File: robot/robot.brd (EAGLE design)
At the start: 58.1 x 41.9 mm, 12 parts, among them Q1 MOSFET-NCHANNELBSS138

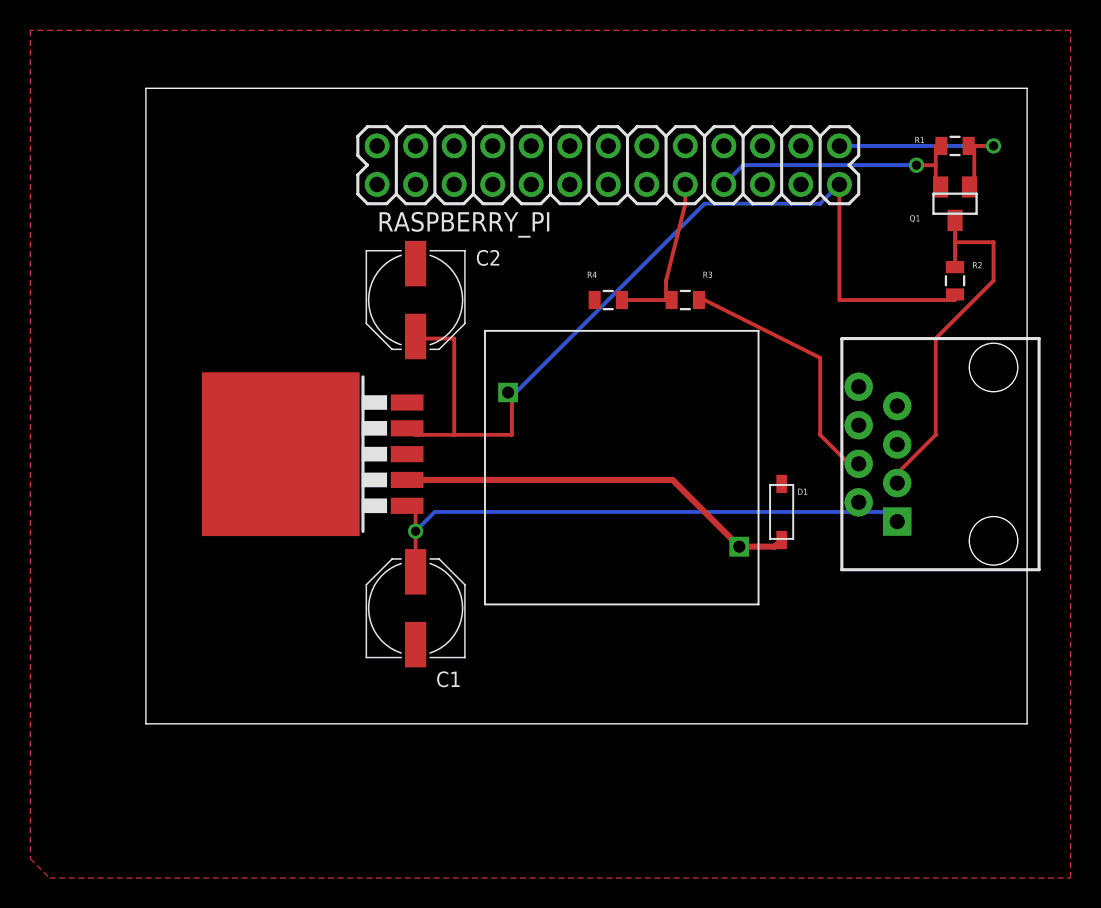
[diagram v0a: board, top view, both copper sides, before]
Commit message: Cleaning up the pcb
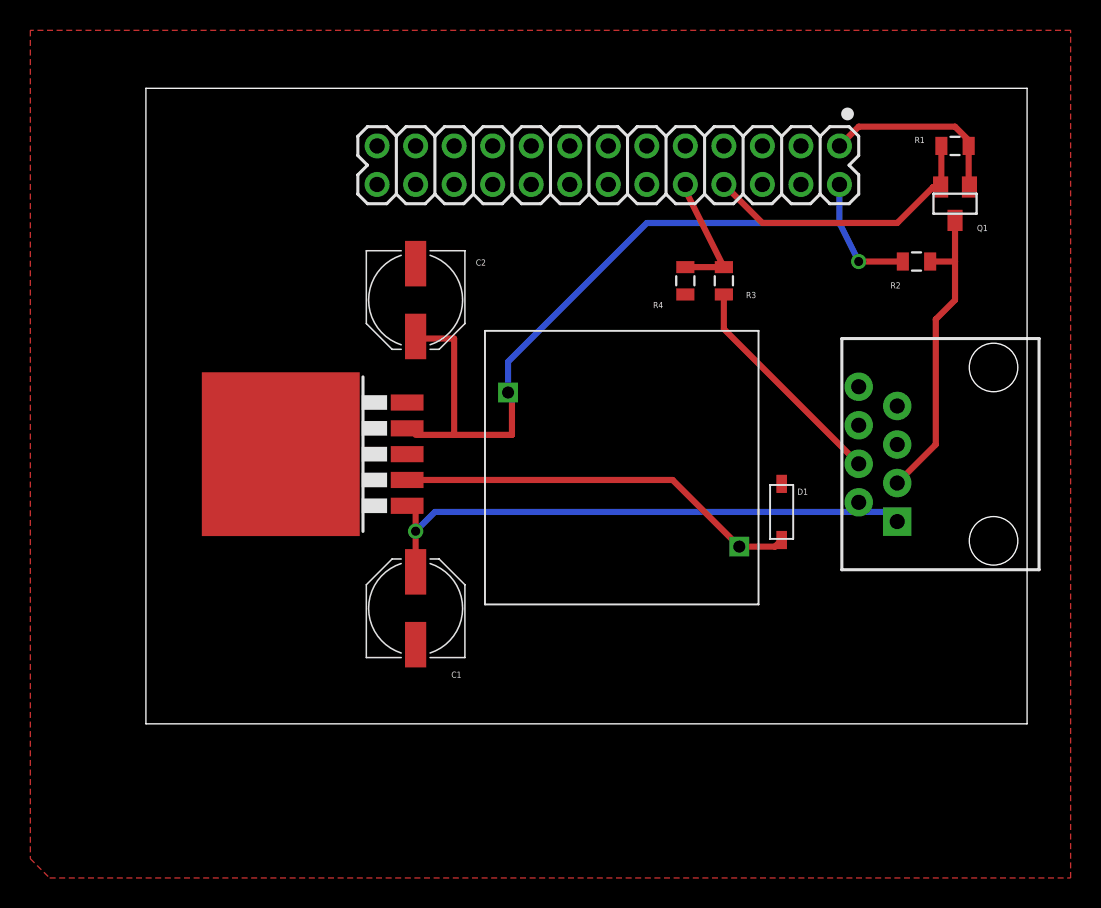
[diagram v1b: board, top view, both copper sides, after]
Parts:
- moved R4 5.24 mm to (38.1, 30.5), turned to 90 degrees
- moved R2 2.84 mm to (53.3, 31.8), turned to 180 degrees
- moved R3 2.84 mm to (40.6, 30.5), turned to 270 degrees
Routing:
- net HV: track 62.3 -> 55.3 mm, vias 0 -> 1
- net TX_HV: track 24.1 -> 20.5 mm
- net RX_HV: track 18.2 -> 15.5 mm
- net RX_LV: track 11.1 -> 8.59 mm
- net LV: track 14.7 -> 12.9 mm, vias 1 -> 0
- net TX_LV: track 17.8 -> 19.1 mm, vias 1 -> 0

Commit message: Made board shorter
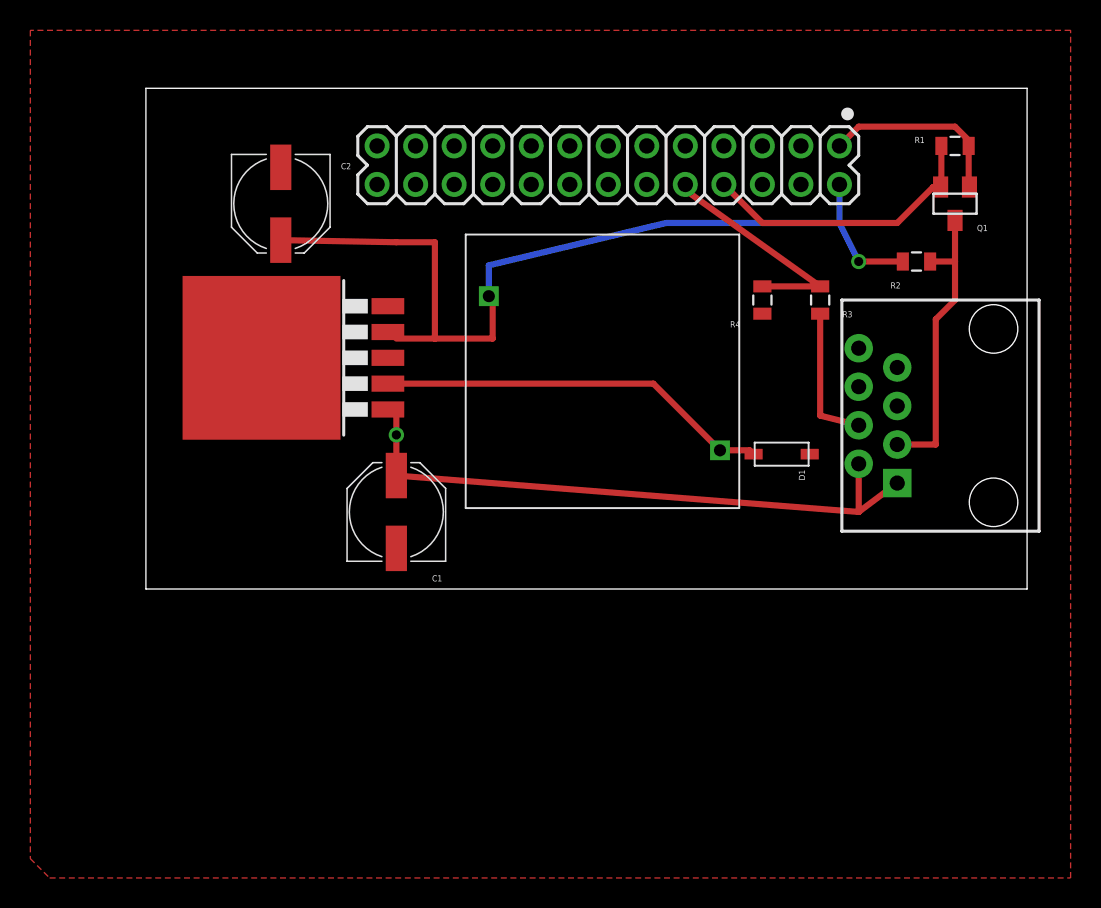
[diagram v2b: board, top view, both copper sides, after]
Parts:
- moved C2 10.9 mm to (11.4, 35.6)
- moved R3 6.48 mm to (47.0, 29.2)
- moved C1 6.48 mm to (19.1, 15.2)
- moved U$1 6.48 mm to (10.2, 25.4)
- moved U$2 6.48 mm to (33.0, 24.1)
- moved R4 5.24 mm to (43.2, 29.2)
- moved D1 3.81 mm to (44.5, 19.1), turned to 0 degrees
- moved IROBOT 2.54 mm to (58.4, 21.6)
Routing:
- net RX_LV: track 8.59 -> 15.1 mm
- net RX_HV: track 15.5 -> 9.34 mm
- net HV: track 55.3 -> 60.6 mm
- net UNREG_12V: track 38.2 -> 41.6 mm
- net TX_HV: track 20.5 -> 19.5 mm
- net N$1: track 26.7 -> 26.0 mm
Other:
- board size 58.1 x 41.9 mm -> 58.1 x 33 mm
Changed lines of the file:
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@@
 <board>
 <plain>
-<wire x1="2.54" y1="1.27" x2="60.63" y2="1.27" width="0" layer="20"/>
-<wire x1="60.63" y1="1.27" x2="60.63" y2="43.17" width="0" layer="20"/>
+<wire x1="2.54" y1="10.16" x2="60.63" y2="10.16" width="0" layer="20"/>
+<wire x1="60.63" y1="10.16" x2="60.63" y2="43.17" width="0" layer="20"/>
 <wire x1="60.63" y1="43.17" x2="2.54" y2="43.17" width="0" layer="20"/>
-<wire x1="2.54" y1="43.17" x2="2.54" y2="1.27" width="0" layer="20"/>
+<wire x1="2.54" y1="43.17" x2="2.54" y2="10.16" width="0" layer="20"/>
 <circle x="48.7934" y="41.4782" radius="0.218496875" width="0.4064" layer="21"/>
 </plain>
@@
 </autorouter>
 <elements>
-<element name="U$1" library="TL2575" package="TO-263" value="TL2575" x="11.43" y="19.05" smashed="yes" rot="R90"/>
-<element name="C1" library="SparkFun-Capacitors" package="PANASONIC_D" value="47uF" x="20.32" y="8.89" smashed="yes" rot="R90">
-<attribute name="NAME" x="23.34" y="4.715" size="0.4064" layer="25" rot="R180"/>
-</element>
-<element name="C2" library="SparkFun-Passives" package="PANASONIC_D" value="220uF" x="20.32" y="29.21" smashed="yes" rot="R270">
-<attribute name="NAME" x="24.285" y="31.48" size="0.4064" layer="25"/>
-</element>
-<element name="U$2" library="PE-52627NL" package="PE-52627NL" value="PE-52627NL" x="34.29" y="17.78" rot="R90"/>
-<element name="D1" library="adafruit" package="SOD-123" value="1A" x="44.45" y="15.24" smashed="yes" rot="R90">
-<attribute name="NAME" x="46.185" y="16.78" size="0.4064" layer="25" rot="R180"/>
-</element>
-<element name="IROBOT" library="SparkFun-Connectors" package="RJ45-8" value="RJ45-8PTH" x="58.42" y="19.05" rot="R90"/>
+<element name="U$1" library="TL2575" package="TO-263" value="TL2575" x="10.16" y="25.4" smashed="yes" rot="R90"/>
+<element name="C1" library="SparkFun-Capacitors" package="PANASONIC_D" value="47uF" x="19.05" y="15.24" smashed="yes" rot="R90">
+<attribute name="NAME" x="22.07" y="11.065" size="0.4064" layer="25" rot="R180"/>
+</element>
+<element name="C2" library="SparkFun-Passives" package="PANASONIC_D" value="220uF" x="11.43" y="35.56" smashed="yes" rot="R270">
+<attribute name="NAME" x="15.395" y="37.83" size="0.4064" layer="25"/>
+</element>
+<element name="U$2" library="PE-52627NL" package="PE-52627NL" value="PE-52627NL" x="33.02" y="24.13" rot="R90"/>
+<element name="D1" library="adafruit" package="SOD-123" value="1A" x="44.45" y="19.05" smashed="yes">
+<attribute name="NAME" x="45.99" y="17.315" size="0.4064" layer="25" rot="R90"/>
+</element>
+<element name="IROBOT" library="SparkFun-Connectors" package="RJ45-8" value="RJ45-8PTH" x="58.42" y="21.59" rot="R90"/>
 <element name="RASPBERRY_PI" library="SparkFun-Connectors" package="2X13" value="M13X22X13" x="48.26" y="39.37" smashed="yes" rot="R180"/>
 <element name="R1" library="SparkFun-Resistors" package="0805" value="10K" x="55.88" y="39.37" smashed="yes">
@@
 <attribute name="NAME" x="51.6255" y="29.972" size="0.4064" layer="25"/>
 </element>
-<element name="R3" library="SparkFun-Resistors" package="0805" value="10K" x="40.64" y="30.48" smashed="yes" rot="R270">
-<attribute name="NAME" x="42.1005" y="29.337" size="0.4064" layer="25"/>
-</element>
-<element name="R4" library="SparkFun-Resistors" package="0805" value="10K" x="38.1" y="30.48" smashed="yes" rot="R90">
-<attribute name="NAME" x="36.6395" y="29.083" size="0.4064" layer="25" rot="R180"/>
+<element name="R3" library="SparkFun-Resistors" package="0805" value="10K" x="46.99" y="29.21" smashed="yes" rot="R270">
+<attribute name="NAME" x="48.4505" y="28.067" size="0.4064" layer="25"/>
+</element>
+<element name="R4" library="SparkFun-Resistors" package="0805" value="10K" x="43.18" y="29.21" smashed="yes" rot="R90">
+<attribute name="NAME" x="41.7195" y="27.813" size="0.4064" layer="25" rot="R180"/>
 </element>
 <element name="Q1" library="SparkFun-DiscreteSemi" package="SOT23" value="MOSFET-NCHANNELBSS138" x="55.88" y="35.56" smashed="yes" rot="R180">
@@
 <contactref element="IROBOT" pad="1"/>
 <contactref element="IROBOT" pad="2"/>
-<wire x1="20.32" y1="11.29" x2="20.32" y2="13.97" width="0.4064" layer="1"/>
-<wire x1="20.32" y1="13.97" x2="20.32" y2="15.24" width="0.4064" layer="1"/>
-<wire x1="20.32" y1="15.24" x2="19.7612" y2="15.6464" width="0.254" layer="1"/>
-<wire x1="52.07" y1="15.24" x2="49.53" y2="15.24" width="0.4064" layer="16"/>
-<wire x1="52.07" y1="15.24" x2="52.07" y2="14.605" width="0.4064" layer="16"/>
-<wire x1="21.59" y1="15.24" x2="20.32" y2="13.97" width="0.4064" layer="16"/>
-<wire x1="49.53" y1="15.24" x2="21.59" y2="15.24" width="0.4064" layer="16"/>
-<wire x1="49.53" y1="15.24" x2="49.53" y2="15.875" width="0.4064" layer="16"/>
-<via x="20.32" y="13.97" extent="1-16" drill="0.6096"/>
+<wire x1="19.05" y1="17.64" x2="19.05" y2="20.32" width="0.4064" layer="1"/>
+<wire x1="19.05" y1="20.32" x2="19.05" y2="21.59" width="0.4064" layer="1"/>
+<wire x1="19.05" y1="21.59" x2="18.4912" y2="21.9964" width="0.254" layer="1"/>
+<via x="19.05" y="20.32" extent="1-16" drill="0.6096"/>
+<wire x1="19.05" y1="17.64" x2="49.53" y2="15.24" width="0.4064" layer="1"/>
+<wire x1="49.53" y1="15.24" x2="49.53" y2="18.415" width="0.4064" layer="1"/>
+<wire x1="52.07" y1="17.145" x2="49.53" y2="15.24" width="0.4064" layer="1"/>
 </signal>
 <signal name="GND">
@@
 <contactref element="D1" pad="C"/>
 <contactref element="U$2" pad="P$1"/>
-<wire x1="19.7612" y1="17.3482" x2="37.2618" y2="17.3482" width="0.4064" layer="1"/>
-<wire x1="37.2618" y1="17.3482" x2="41.656" y2="12.954" width="0.4064" layer="1"/>
-<wire x1="41.656" y1="12.954" x2="44.014" y2="12.954" width="0.4064" layer="1"/>
-<wire x1="44.014" y1="12.954" x2="44.45" y2="13.39" width="0.4064" layer="1"/>
+<wire x1="18.4912" y1="23.6982" x2="35.9918" y2="23.6982" width="0.4064" layer="1"/>
+<wire x1="35.9918" y1="23.6982" x2="40.386" y2="19.304" width="0.4064" layer="1"/>
+<wire x1="40.386" y1="19.304" x2="42.346" y2="19.304" width="0.4064" layer="1"/>
+<wire x1="42.346" y1="19.304" x2="42.6" y2="19.05" width="0.4064" layer="1"/>
 </signal>
 <signal name="RX_LV">
@@
 <contactref element="R4" pad="2"/>
 <contactref element="RASPBERRY_PI" pad="10"/>
-<wire x1="40.64" y1="31.38" x2="38.1" y2="31.38" width="0.4064" layer="1"/>
-<wire x1="40.64" y1="31.38" x2="38.1" y2="36.46" width="0.4064" layer="1"/>
+<wire x1="46.99" y1="30.11" x2="43.18" y2="30.11" width="0.4064" layer="1"/>
+<wire x1="46.99" y1="30.11" x2="38.1" y2="36.46" width="0.4064" layer="1"/>
 <wire x1="38.1" y1="36.46" x2="38.1" y2="36.83" width="0.4064" layer="1"/>
 </signal>
@@
 <wire x1="55.88" y1="29.21" x2="54.61" y2="27.94" width="0.4064" layer="1"/>
 <wire x1="54.61" y1="27.94" x2="54.61" y2="19.685" width="0.4064" layer="1"/>
-<wire x1="54.61" y1="19.685" x2="52.07" y2="17.145" width="0.4064" layer="1"/>
+<wire x1="54.61" y1="19.685" x2="52.07" y2="19.685" width="0.4064" layer="1"/>
 <wire x1="55.88" y1="34.46" x2="55.88" y2="31.75" width="0.4064" layer="1"/>
 <wire x1="55.88" y1="31.75" x2="54.24" y2="31.75" width="0.4064" layer="1"/>
@@
 <contactref element="C2" pad="+"/>
 <contactref element="U$2" pad="P$2"/>
-<wire x1="26.67" y1="20.32" x2="22.86" y2="20.32" width="0.4064" layer="1"/>
-<wire x1="22.86" y1="20.32" x2="20.32" y2="20.32" width="0.4064" layer="1"/>
-<wire x1="26.67" y1="22.86" x2="26.67" y2="20.32" width="0.4064" layer="1"/>
-<wire x1="20.32" y1="20.32" x2="19.7612" y2="20.7518" width="0.254" layer="1"/>
-<wire x1="26.67" y1="22.86" x2="26.416" y2="23.114" width="0.4064" layer="1"/>
-<wire x1="22.86" y1="26.67" x2="20.32" y2="26.67" width="0.4064" layer="1"/>
-<wire x1="22.86" y1="20.32" x2="22.86" y2="26.67" width="0.4064" layer="1"/>
-<wire x1="20.32" y1="26.67" x2="20.32" y2="26.81" width="0.254" layer="1"/>
-<wire x1="26.67" y1="22.86" x2="26.416" y2="23.114" width="0.254" layer="16"/>
+<wire x1="25.4" y1="26.67" x2="21.59" y2="26.67" width="0.4064" layer="1"/>
+<wire x1="21.59" y1="26.67" x2="19.05" y2="26.67" width="0.4064" layer="1"/>
+<wire x1="25.4" y1="29.21" x2="25.4" y2="26.67" width="0.4064" layer="1"/>
+<wire x1="19.05" y1="26.67" x2="18.4912" y2="27.1018" width="0.254" layer="1"/>
+<wire x1="25.4" y1="29.21" x2="25.146" y2="29.464" width="0.4064" layer="1"/>
+<wire x1="21.59" y1="33.02" x2="19.05" y2="33.02" width="0.4064" layer="1"/>
+<wire x1="21.59" y1="26.67" x2="21.59" y2="33.02" width="0.4064" layer="1"/>
+<wire x1="19.05" y1="33.02" x2="11.43" y2="33.16" width="0.4064" layer="1"/>
+<wire x1="25.4" y1="29.21" x2="25.146" y2="29.464" width="0.254" layer="16"/>
 <wire x1="52.44" y1="31.75" x2="49.53" y2="31.75" width="0.4064" layer="1"/>
 <via x="49.53" y="31.75" extent="1-16" drill="0.6"/>
 <wire x1="49.53" y1="31.75" x2="48.26" y2="34.29" width="0.4064" layer="16"/>
 <wire x1="48.26" y1="34.29" x2="48.26" y2="36.83" width="0.4064" layer="16"/>
-<wire x1="48.26" y1="34.29" x2="35.56" y2="34.29" width="0.4064" layer="16"/>
-<wire x1="35.56" y1="34.29" x2="26.416" y2="25.146" width="0.4064" layer="16"/>
-<wire x1="26.416" y1="25.146" x2="26.416" y2="23.114" width="0.4064" layer="16"/>
+<wire x1="48.26" y1="34.29" x2="36.83" y2="34.29" width="0.4064" layer="16"/>
+<wire x1="36.83" y1="34.29" x2="25.146" y2="31.496" width="0.4064" layer="16"/>
+<wire x1="25.146" y1="31.496" x2="25.146" y2="29.464" width="0.4064" layer="16"/>
 </signal>
 <signal name="RX_HV">
 <contactref element="R3" pad="2"/>
 <contactref element="IROBOT" pad="4"/>
-<wire x1="48.895" y1="18.415" x2="49.53" y2="18.415" width="0.4064" layer="1"/>
-<wire x1="40.64" y1="29.58" x2="40.64" y2="27.305" width="0.4064" layer="1"/>
-<wire x1="40.64" y1="27.305" x2="49.53" y2="18.415" width="0.4064" layer="1"/>
+<wire x1="46.99" y1="28.31" x2="46.99" y2="21.59" width="0.4064" layer="1"/>
+<wire x1="46.99" y1="21.59" x2="49.53" y2="20.955" width="0.4064" layer="1"/>
 </signal>
 </signals>

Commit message: Add drill holes and graphic
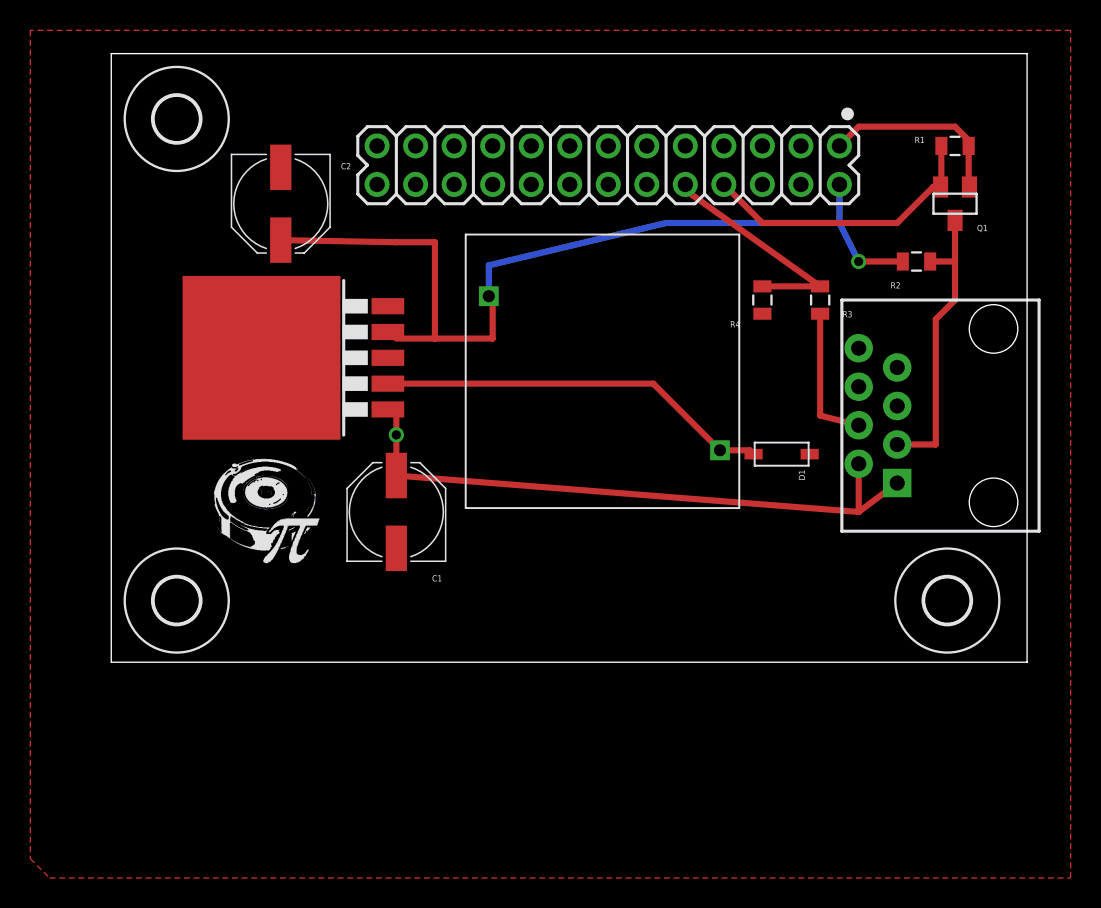
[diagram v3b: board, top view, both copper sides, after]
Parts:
- added U$3, U$5, U$6: (no value), holes:3,0
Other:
- board size 58.1 x 33 mm -> 60.4 x 40.1 mm
- board text added: "/Users/tcasselman/code/pi/fido_pi/graphic.bmp"
